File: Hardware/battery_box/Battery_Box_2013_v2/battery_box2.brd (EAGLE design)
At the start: 60 x 80 mm, 49 parts, among them IC1 AD826R, IC2 LM2574, IC3 PIC16F1824, IC4 LD117AS18TR, J1 CON_HEADER_PRG_PIC_ICSPA, Q1 IRFR5505PBFTO252, Q2 BSS123, X1 CON_MOLEX_39_29_1028, X2 KUSBVX

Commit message: added pdf of schematic
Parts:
- C3: value 22u -> 220u
- C6: device resistor:C0805 -> rcl:C0402
- R14, R15: value 66k -> 66k5
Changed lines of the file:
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@@
 <layer number="14" name="Route14" color="1" fill="6" visible="no" active="no"/>
 <layer number="15" name="Route15" color="4" fill="6" visible="no" active="no"/>
-<layer number="16" name="Bottom" color="1" fill="1" visible="yes" active="yes"/>
+<layer number="16" name="Bottom" color="1" fill="1" visible="no" active="yes"/>
 <layer number="17" name="Pads" color="2" fill="1" visible="yes" active="yes"/>
 <layer number="18" name="Vias" color="13" fill="1" visible="yes" active="yes"/>
@@
 <layer number="20" name="Dimension" color="15" fill="1" visible="yes" active="yes"/>
 <layer number="21" name="tPlace" color="7" fill="1" visible="yes" active="yes"/>
-<layer number="22" name="bPlace" color="7" fill="1" visible="yes" active="yes"/>
-<layer number="23" name="tOrigins" color="15" fill="1" visible="yes" active="yes"/>
+<layer number="22" name="bPlace" color="7" fill="1" visible="no" active="yes"/>
+<layer number="23" name="tOrigins" color="15" fill="1" visible="no" active="yes"/>
 <layer number="24" name="bOrigins" color="15" fill="1" visible="yes" active="yes"/>
 <layer number="25" name="tNames" color="7" fill="1" visible="yes" active="yes"/>
-<layer number="26" name="bNames" color="7" fill="1" visible="yes" active="yes"/>
-<layer number="27" name="tValues" color="7" fill="1" visible="yes" active="yes"/>
-<layer number="28" name="bValues" color="7" fill="1" visible="yes" active="yes"/>
+<layer number="26" name="bNames" color="7" fill="1" visible="no" active="yes"/>
+<layer number="27" name="tValues" color="7" fill="1" visible="no" active="yes"/>
+<layer number="28" name="bValues" color="7" fill="1" visible="no" active="yes"/>
 <layer number="29" name="tStop" color="7" fill="3" visible="no" active="yes"/>
 <layer number="30" name="bStop" color="7" fill="6" visible="no" active="yes"/>
@@
 <layer number="42" name="bRestrict" color="1" fill="10" visible="no" active="yes"/>
 <layer number="43" name="vRestrict" color="2" fill="10" visible="no" active="yes"/>
-<layer number="44" name="Drills" color="7" fill="1" visible="yes" active="yes"/>
+<layer number="44" name="Drills" color="7" fill="1" visible="no" active="yes"/>
 <layer number="45" name="Holes" color="7" fill="1" visible="no" active="yes"/>
 <layer number="46" name="Milling" color="3" fill="1" visible="no" active="yes"/>
@@
 <layer number="49" name="Reference" color="7" fill="1" visible="no" active="yes"/>
 <layer number="50" name="dxf" color="7" fill="1" visible="no" active="no"/>
-<layer number="51" name="tDocu" color="14" fill="1" visible="yes" active="yes"/>
+<layer number="51" name="tDocu" color="14" fill="1" visible="no" active="yes"/>
 <layer number="52" name="bDocu" color="7" fill="1" visible="no" active="yes"/>
 <layer number="53" name="tGND_GNDA" color="7" fill="1" visible="no" active="no"/>
@@
 <attribute name="VALUE" x="46.54" y="4.73" size="1.27" layer="27" rot="R90"/>
 </element>
-<element name="C3" library="rcl" package="C0805" value="22u" x="24" y="7" smashed="yes" rot="R270">
+<element name="C3" library="rcl" package="C0805" value="220u" x="24" y="7" smashed="yes" rot="R270">
 <attribute name="NAME" x="25.27" y="8.27" size="1.27" layer="25" font="vector" rot="R270"/>
 <attribute name="VALUE" x="21.46" y="8.27" size="1.27" layer="27" rot="R270"/>
@@
 <attribute name="VALUE" x="54.365" y="37.46" size="1.27" layer="27"/>
 </element>
-<element name="R14" library="rcl" package="R0805" value="66k" x="55" y="34" smashed="yes" rot="R90">
+<element name="R14" library="rcl" package="R0805" value="66k5" x="55" y="34" smashed="yes" rot="R90">
 <attribute name="NAME" x="57.93" y="32.165" size="1.27" layer="25" font="vector" rot="R90"/>
 <attribute name="VALUE" x="57.54" y="33.365" size="1.27" layer="27" rot="R90"/>
 </element>
-<element name="R15" library="rcl" package="R0805" value="66k" x="45" y="32" smashed="yes" rot="R270">
+<element name="R15" library="rcl" package="R0805" value="66k5" x="45" y="32" smashed="yes" rot="R270">
 <attribute name="NAME" x="42.47" y="33.635" size="1.27" layer="25" font="vector" rot="R270"/>
 <attribute name="VALUE" x="42.46" y="32.635" size="1.27" layer="27" rot="R270"/>
@@
 <attribute name="VALUE" x="11.841" y="3.571" size="1.27" layer="27"/>
 </element>
-<element name="C6" library="resistor" package="C0805" value="100n" x="41" y="60" smashed="yes" rot="R270">
-<attribute name="NAME" x="41.984" y="55.511" size="1.27" layer="25" rot="R90"/>
+<element name="C6" library="rcl" package="C0402" value="100n" x="41" y="60" smashed="yes" rot="R270">
+<attribute name="NAME" x="42.489" y="56.984" size="1.27" layer="25" rot="R180"/>
 <attribute name="VALUE" x="38.714" y="60.889" size="1.27" layer="27" rot="R270"/>
 </element>
@@
 <wire x1="34.21" y1="61" x2="33.81" y2="60.6" width="0.4064" layer="1"/>
 <wire x1="36" y1="66.05" x2="36" y2="61" width="0.6096" layer="1"/>
-<wire x1="41" y1="60.85" x2="38.1" y2="60.85" width="0.4064" layer="1"/>
+<wire x1="41" y1="60.65" x2="38.1" y2="60.85" width="0.4064" layer="1"/>
 <wire x1="38.1" y1="60.85" x2="38" y2="60.95" width="0.4064" layer="1"/>
 <wire x1="36" y1="66.05" x2="37.465" y2="66.05" width="0.8128" layer="1"/>
@@
 </signal>
 </signals>
-<errors>
-</errors>
 </board>
 </drawing>

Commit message: updated C3 footprint and component values/cost
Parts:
- C1: value (none) -> 1u, 16V
- C2: device rcl:C0805 -> rcl:C1210
- C3: device rcl:C0805 -> rcl:PANASONIC_E
- moved C3 2.24 mm to (23.0, 9.00), turned to 90 degrees
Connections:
- net GND_OUTPUT: now also C3.-; no longer C3.2
- net USB_OUT: now also C3.+; no longer C3.1
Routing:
- net USB_OUT: track 117.5 -> 115.6 mm
- net GND_OUTPUT: track 54.6 -> 55.4 mm
- net N$9: track 70.6 -> 71.4 mm
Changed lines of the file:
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@@
 <layer number="21" name="tPlace" color="7" fill="1" visible="yes" active="yes"/>
 <layer number="22" name="bPlace" color="7" fill="1" visible="no" active="yes"/>
-<layer number="23" name="tOrigins" color="15" fill="1" visible="no" active="yes"/>
+<layer number="23" name="tOrigins" color="15" fill="1" visible="yes" active="yes"/>
 <layer number="24" name="bOrigins" color="15" fill="1" visible="yes" active="yes"/>
 <layer number="25" name="tNames" color="7" fill="1" visible="yes" active="yes"/>
@@
 <attribute name="VALUE" x="18.935" y="77.54" size="1.27" layer="27" rot="R180"/>
 </element>
-<element name="C1" library="rcl" package="C0805" value="" x="18.3" y="72" smashed="yes">
+<element name="C1" library="rcl" package="C0805" value="1u, 16V" x="18.3" y="72" smashed="yes">
 <attribute name="NAME" x="16.07" y="72.63" size="1.27" layer="25" rot="R180"/>
 <attribute name="VALUE" x="17.03" y="69.46" size="1.27" layer="27"/>
 </element>
 <element name="IC2" library="equinox" package="SO14W" value="LM2574" x="34" y="8" smashed="yes" rot="R270">
-<attribute name="NAME" x="37.19" y="1.27" size="1.27" layer="25" font="vector"/>
+<attribute name="NAME" x="36.19" y="13.27" size="1.27" layer="25" font="vector"/>
 <attribute name="VALUE" x="29.19" y="1.46" size="1.27" layer="27"/>
 </element>
-<element name="C2" library="rcl" package="C0805" value="22u" x="44" y="6" smashed="yes" rot="R90">
+<element name="C2" library="rcl" package="C1210" value="22u" x="44" y="6" smashed="yes" rot="R90">
 <attribute name="NAME" x="42.73" y="4.73" size="1.27" layer="25" font="vector" rot="R90"/>
 <attribute name="VALUE" x="46.54" y="4.73" size="1.27" layer="27" rot="R90"/>
 </element>
-<element name="C3" library="rcl" package="C0805" value="220u" x="24" y="7" smashed="yes" rot="R270">
-<attribute name="NAME" x="25.27" y="8.27" size="1.27" layer="25" font="vector" rot="R270"/>
-<attribute name="VALUE" x="21.46" y="8.27" size="1.27" layer="27" rot="R270"/>
+<element name="C3" library="rcl" package="PANASONIC_E" value="220u" x="23" y="9" smashed="yes" rot="R90">
+<attribute name="NAME" x="17.73" y="12.73" size="1.27" layer="25" font="vector" rot="R180"/>
+<attribute name="VALUE" x="25.54" y="7.73" size="1.27" layer="27" rot="R90"/>
 </element>
 <element name="L1" library="equinox" package="SMD_INDUCTOR" value="INDUCTOR" x="8" y="25" smashed="yes" rot="R90">
@@
 </signal>
 <signal name="USB_OUT">
-<contactref element="C3" pad="1"/>
+<contactref element="C3" pad="+"/>
 <contactref element="IC2" pad="3"/>
 <contactref element="L1" pad="P$2"/>
@@
 <wire x1="49.05" y1="40" x2="49.05" y2="34.645" width="0.6096" layer="1"/>
 <wire x1="49.05" y1="34.645" x2="49.095" y2="34.6" width="0.6096" layer="1"/>
-<wire x1="27.305" y1="11.43" x2="24.13" y2="8.255" width="0.381" layer="1"/>
-<wire x1="27.305" y1="12.065" x2="27.305" y2="11.43" width="0.381" layer="1"/>
-<wire x1="32.385" y1="17.145" x2="27.305" y2="12.065" width="0.381" layer="1"/>
-<wire x1="24.13" y1="8.255" x2="24" y2="7.95" width="0.381" layer="1"/>
+<wire x1="23.305" y1="12.43" x2="23.13" y2="12.255" width="0.381" layer="1"/>
+<wire x1="26.305" y1="14.065" x2="23.305" y2="12.43" width="0.381" layer="1"/>
+<wire x1="32.385" y1="17.145" x2="26.305" y2="14.065" width="0.381" layer="1"/>
+<wire x1="23.13" y1="12.255" x2="23" y2="12" width="0.381" layer="1"/>
 <wire x1="32.385" y1="17.145" x2="33" y2="17.145" width="0.381" layer="1"/>
 <wire x1="46.355" y1="35.56" x2="48.895" y2="35.56" width="0.381" layer="1"/>
@@
 <wire x1="9" y1="16.6" x2="8.5" y2="17.1" width="1.6764" layer="1"/>
 <wire x1="11.8" y1="7" x2="11.8" y2="3.2" width="1.4224" layer="1"/>
-<wire x1="11.8" y1="3.2" x2="12.6" y2="2.4" width="1.4224" layer="1"/>
-<wire x1="12.6" y1="2.4" x2="47.4" y2="2.4" width="1.4224" layer="1"/>
-<wire x1="47.4" y1="2.4" x2="49" y2="4" width="1.4224" layer="1"/>
+<wire x1="11.8" y1="3.2" x2="13.3" y2="2" width="1.4224" layer="1"/>
+<wire x1="13.3" y1="2" x2="48.1" y2="2" width="1.4224" layer="1"/>
+<wire x1="48.1" y1="2" x2="49" y2="4" width="1.4224" layer="1"/>
 <wire x1="49" y1="4" x2="49" y2="9" width="1.4224" layer="1"/>
 <wire x1="38.6" y1="9.27" x2="41.27" y2="9.27" width="0.6096" layer="1"/>
@@
 <wire x1="40.27" y1="6.73" x2="42" y2="5" width="0.6096" layer="1"/>
 <wire x1="42" y1="5" x2="43.95" y2="5" width="0.6096" layer="1"/>
-<wire x1="43.95" y1="5" x2="44" y2="5.05" width="0.6096" layer="1"/>
+<wire x1="43.95" y1="5" x2="44" y2="4.6" width="0.6096" layer="1"/>
 <wire x1="47.5" y1="60" x2="47.5" y2="59.5" width="1.6764" layer="1"/>
 <wire x1="47.5" y1="59.5" x2="41" y2="51" width="1.6764" layer="1"/>
@@
 <contactref element="IC2" pad="5"/>
 <contactref element="C2" pad="2"/>
-<contactref element="C3" pad="2"/>
+<contactref element="C3" pad="-"/>
 <contactref element="R2" pad="1"/>
 <contactref element="R4" pad="1"/>
@@
 </polygon>
 <contactref element="D1" pad="A"/>
-<wire x1="16.2" y1="7" x2="20" y2="7" width="0.8128" layer="1"/>
-<wire x1="20" y1="7" x2="21" y2="6" width="0.8128" layer="1"/>
-<wire x1="21" y1="6" x2="23.95" y2="6" width="0.8128" layer="1"/>
-<wire x1="23.95" y1="6" x2="24" y2="6.05" width="0.8128" layer="1"/>
-<wire x1="21.345" y1="15.53" x2="21.345" y2="6.345" width="0.8128" layer="1"/>
-<wire x1="21.345" y1="6.345" x2="21" y2="6" width="0.8128" layer="1"/>
-<wire x1="29.4" y1="5.46" x2="27" y2="5.46" width="0.6096" layer="1"/>
-<wire x1="27" y1="5.46" x2="24.59" y2="5.46" width="0.6096" layer="1"/>
-<wire x1="24.59" y1="5.46" x2="24" y2="6.05" width="0.6096" layer="1"/>
-<wire x1="29.4" y1="6.73" x2="28.27" y2="6.73" width="0.6096" layer="1"/>
-<wire x1="28.27" y1="6.73" x2="27" y2="5.46" width="0.6096" layer="1"/>
-<wire x1="29.4" y1="8" x2="29.4" y2="7.86" width="0.6096" layer="1"/>
-<wire x1="29.4" y1="7.86" x2="28.27" y2="6.73" width="0.6096" layer="1"/>
-<wire x1="44" y1="6.95" x2="46.05" y2="6.95" width="0.6096" layer="1"/>
+<wire x1="16.2" y1="7" x2="19.4" y2="6" width="0.8128" layer="1"/>
+<wire x1="19.4" y1="6" x2="23" y2="6" width="0.8128" layer="1"/>
+<wire x1="21.345" y1="15.53" x2="19.345" y2="15.445" width="0.8128" layer="1"/>
+<wire x1="19.345" y1="15.445" x2="19.4" y2="6" width="0.8128" layer="1"/>
+<wire x1="29.4" y1="5.46" x2="29.39" y2="5.66" width="0.6096" layer="1"/>
+<wire x1="29.34" y1="6.3" x2="29.39" y2="5.66" width="0.6096" layer="1"/>
+<wire x1="29.39" y1="5.66" x2="23" y2="6" width="0.6096" layer="1"/>
+<wire x1="29.4" y1="6.73" x2="29.33" y2="7.37" width="0.6096" layer="1"/>
+<wire x1="29.33" y1="7.37" x2="29.34" y2="6.3" width="0.6096" layer="1"/>
+<wire x1="29.4" y1="8" x2="29.4" y2="6.86" width="0.6096" layer="1"/>
+<wire x1="29.4" y1="6.86" x2="29.33" y2="7.37" width="0.6096" layer="1"/>
+<wire x1="44" y1="7.4" x2="46.05" y2="6.95" width="0.6096" layer="1"/>
 <wire x1="46.05" y1="6.95" x2="46.1" y2="7" width="0.6096" layer="1"/>
 <via x="46.1" y="7" extent="1-16" drill="0.6" diameter="1.016"/>

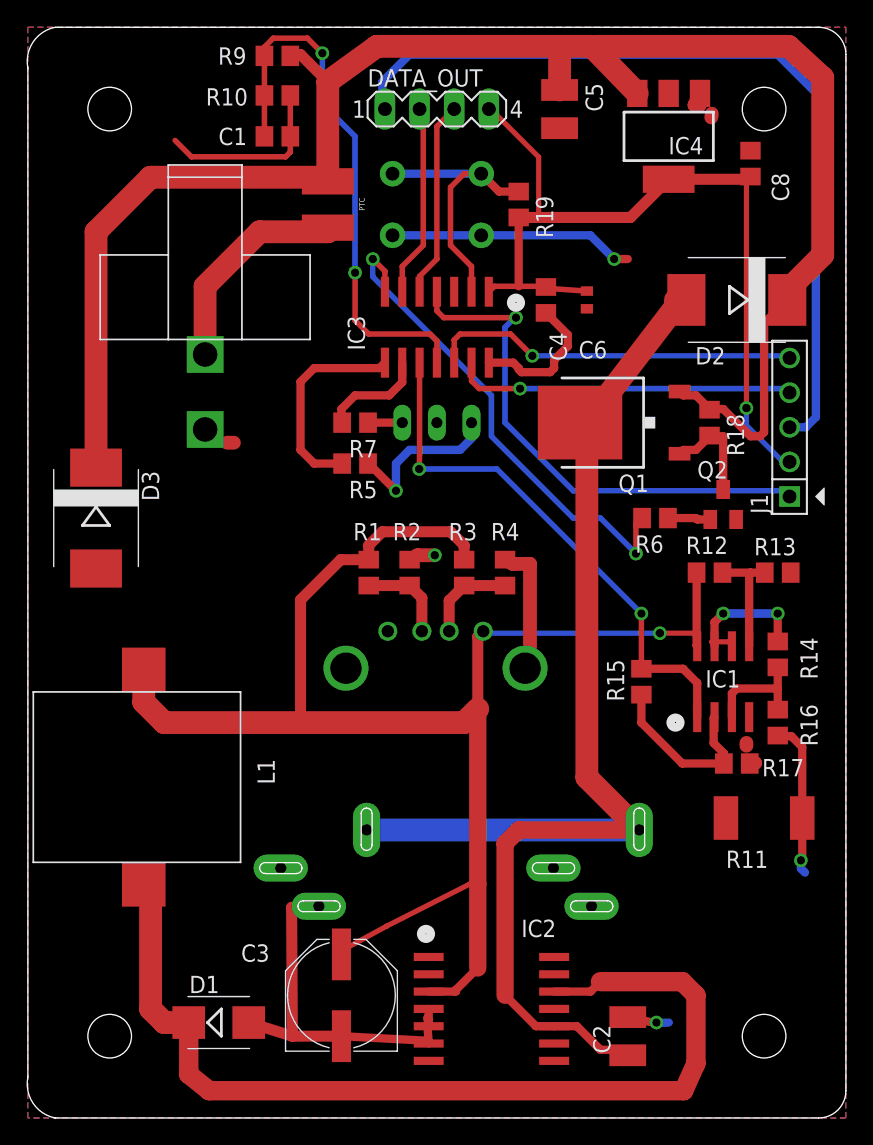
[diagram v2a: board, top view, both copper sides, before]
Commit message: Most recent Gerbers
Most recent footprints and testpoints added.
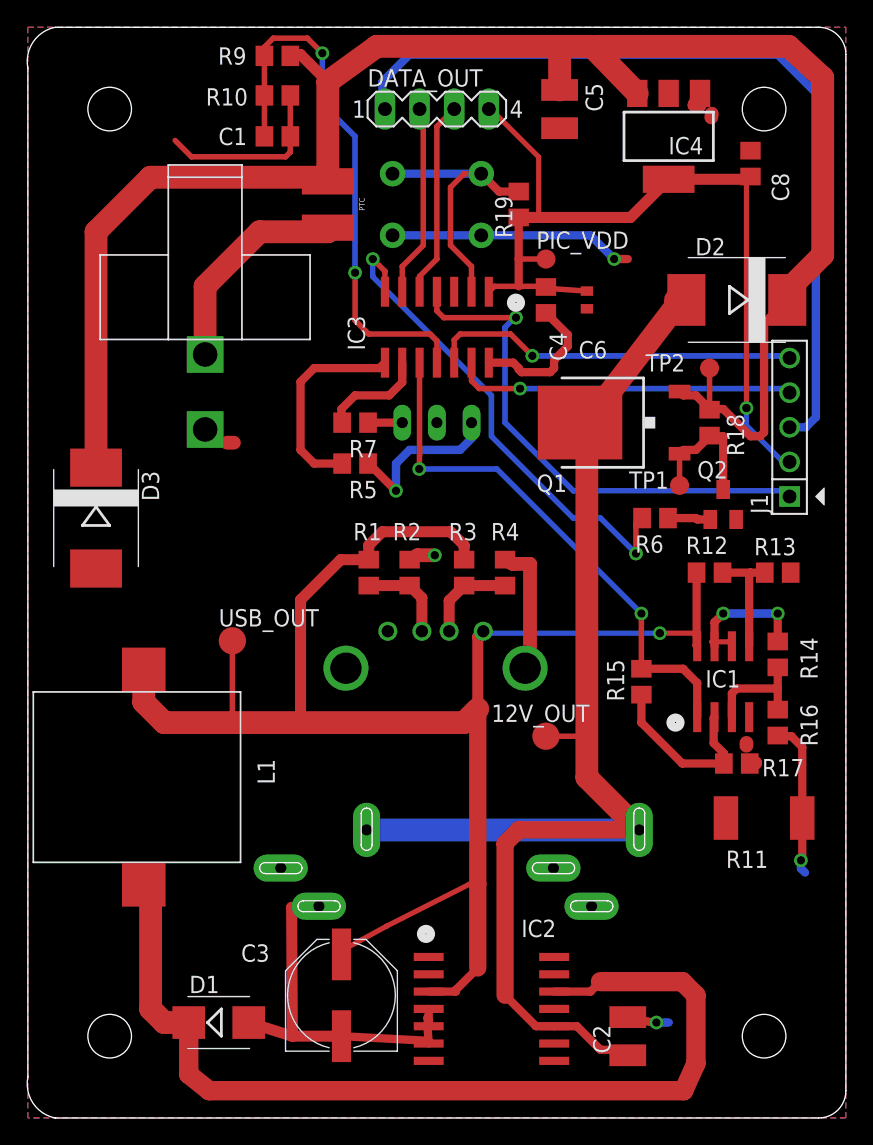
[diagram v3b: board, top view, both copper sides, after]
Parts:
- added 12V_OUT, USB_OUT: TPTP20R, testpad:TP20R
- added PIC_VDD, TP1, TP2: TPTP14R, testpad:TP14R
- renumbered X2 to USB
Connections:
- net 12V_OUT: now also 12V_OUT.TP
- net N$11: now also TP1.TP
- net USB_OUT: now also USB_OUT.TP
- net VDD: now also PIC_VDD.TP
- net V_BATT: now also TP2.TP
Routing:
- net 12V_OUT: track 97.6 -> 103.6 mm
- net USB_OUT: track 115.6 -> 121.6 mm
- net V_BATT: track 129.5 -> 132.5 mm
- net N$11: track 7.68 -> 10.0 mm
- net VDD: track 62.8 -> 64.8 mm
